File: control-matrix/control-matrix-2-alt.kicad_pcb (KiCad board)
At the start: 2 copper layers, 44 x 30 mm, 9 parts, among them J1 Screw_Terminal_01x02, J2 Screw_Terminal_01x02, J9 Screw_Terminal_01x02, SW1 SW_SPDT

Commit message: control-matrix: add power input labels on silkscreen
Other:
- board text added: "GND +12V"
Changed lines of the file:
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@@
 		(layer "Edge.Cuts")
+	)
+	(gr_text "GND  +12V"
+		(at 91.3 81.7 0)
+		(layer "F.SilkS")
+		(effects
+			(font
+				(size 1 1)
+				(thickness 0.2)
+				(bold yes)
+			)
+			(justify left bottom)
+		)
 	)
 	(segment

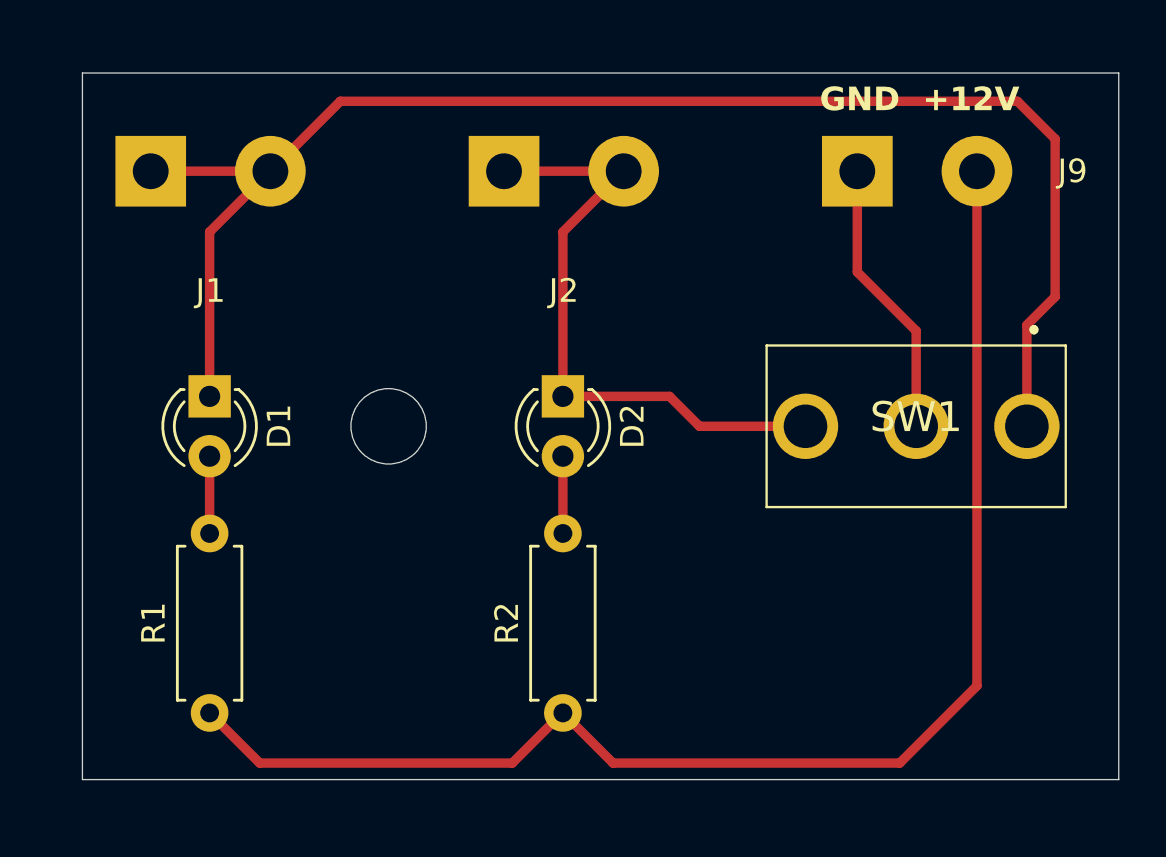
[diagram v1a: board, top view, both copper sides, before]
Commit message: control-matrix: 2-alt: move switch to center of board
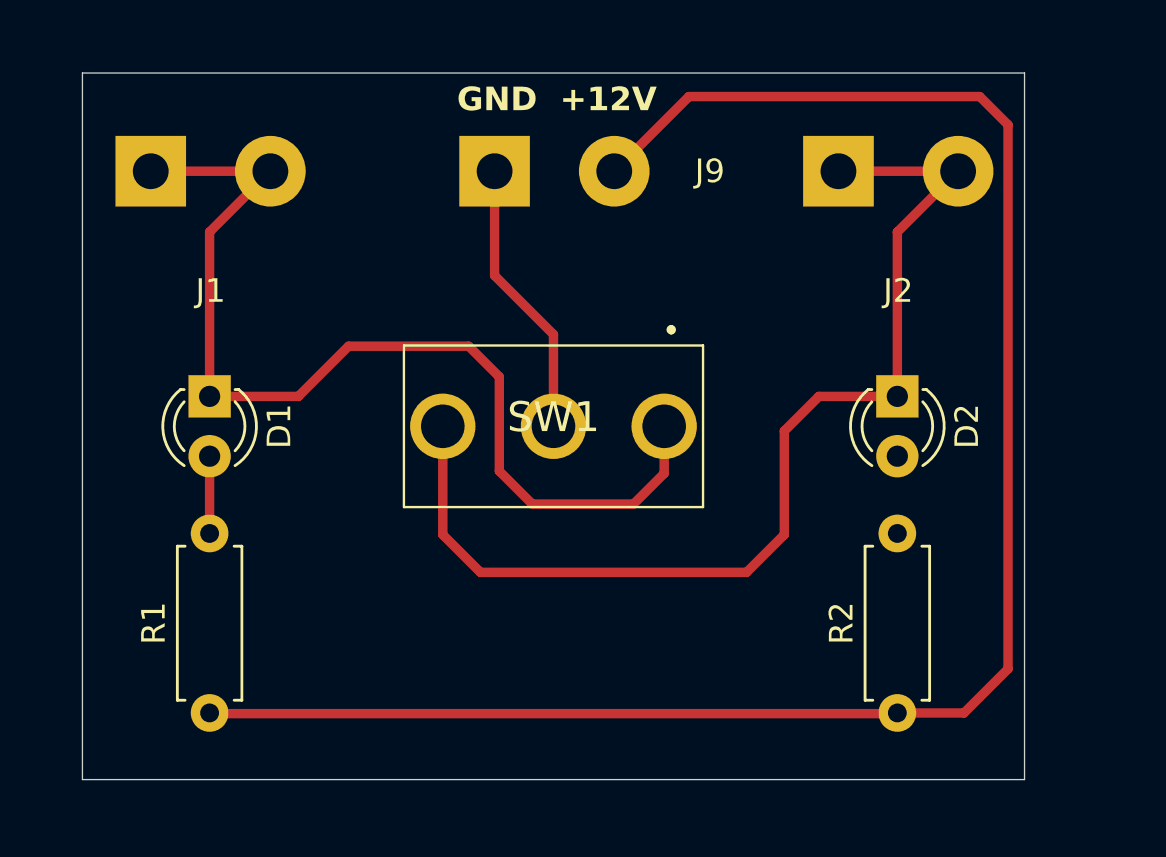
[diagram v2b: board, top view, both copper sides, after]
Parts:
- removed H1: MountingHole, MountingHole:MountingHole_3.2mm_M3
- moved J9 15.4 mm to (77.5, 84.2)
- moved SW1 15.4 mm to (84.7, 95.0)
- moved D2 14.2 mm to (94.6, 93.7)
- moved J2 14.2 mm to (92.1, 84.2)
- moved R2 14.2 mm to (94.6, 107.2)
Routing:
- net Net-(D1-K): track 63.6 -> 43.5 mm
- net Net-(D2-K): track 26.5 -> 45.9 mm
- net +12V: track 58.4 -> 76.3 mm
- net Net-(D2-A): track 3.28 -> 0.00 mm
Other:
- board size 44 x 30 mm -> 40 x 30 mm

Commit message: control-matrix: add ground planes
This avoids having to etch too much copper.
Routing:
- net GND: track 11.9 -> 0.00 mm
- added copper zone on F.Cu, net GND
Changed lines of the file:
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@@
-	)
-	(segment
-		(start 80 95)
-		(end 80 91.1)
-		(width 0.4)
-		(layer "F.Cu")
-		(net 5)
-	)
-	(segment
-		(start 80 91.1)
-		(end 77.5 88.6)
-		(width 0.4)
-		(layer "F.Cu")
-		(net 5)
-	)
-	(segment
-		(start 77.5 88.6)
-		(end 77.5 84.17)
-		(width 0.4)
-		(layer "F.Cu")
-		(net 5)
 	)
 	(segment
@@
 		(net 6)
 	)
+	(zone
+		(net 5)
+		(net_name "GND")
+		(layer "F.Cu")
+		(hatch edge 0.5)
+		(connect_pads
+			(clearance 0.5)
+		)
+		(min_thickness 0.25)
+		(filled_areas_thickness no)
+		(fill yes
+			(thermal_gap 0.5)
+			(thermal_bridge_width 0.5)
+		)
+		(polygon
+			(pts
+				(xy 58.9 78.9) (xy 101.2 79) (xy 100.9 111.3) (xy 58.5 110.5)
+			)
+		)
+	)
 	(embedded_fonts no)
